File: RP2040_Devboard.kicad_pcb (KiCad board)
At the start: 2 copper layers, 42.2 x 59 mm, 47 parts, among them J1 USB_B_Mini, J2 Conn_01x03_Socket, J4 Conn_01x16, J6 Conn_01x16, SW1 SW_Push, SW2 SW_Push, U1 RP2040, U2 AP2112K-1.2, U3 USBLC6-2SC6, U4 W25Q128JVS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

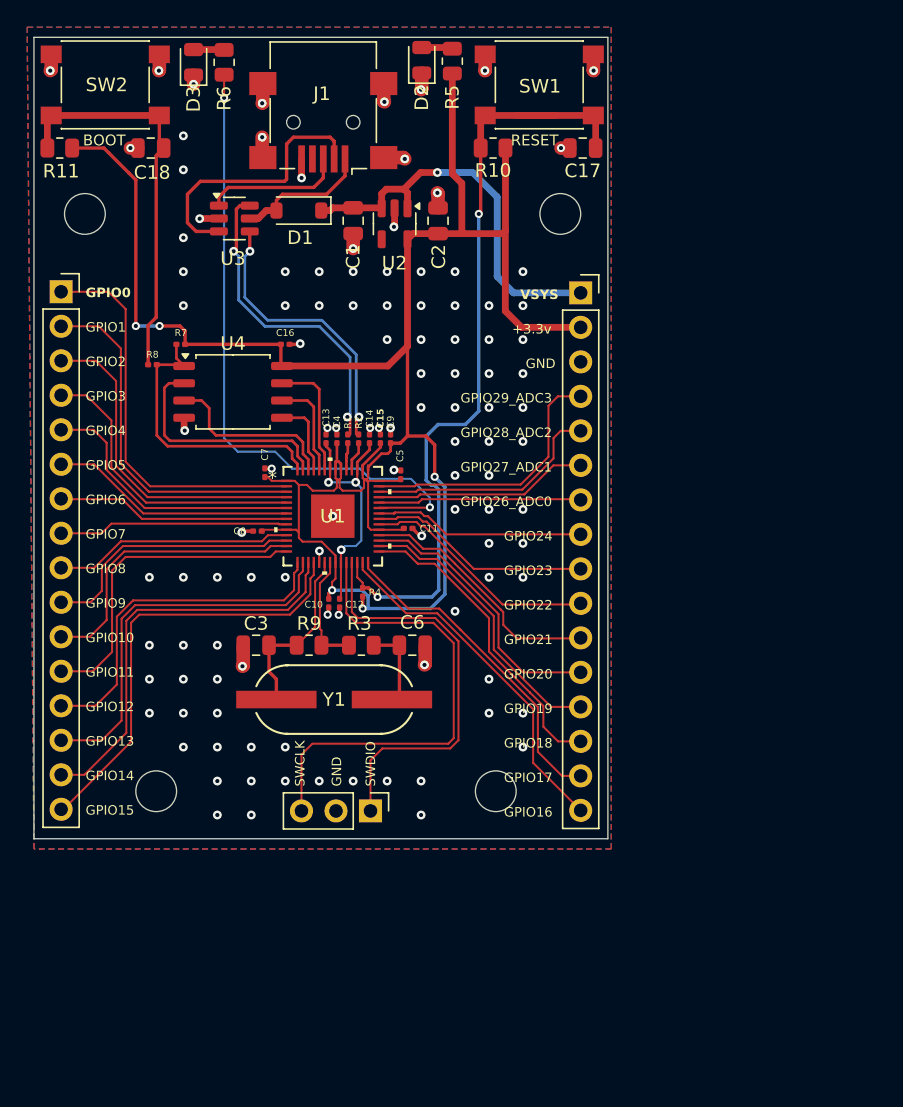
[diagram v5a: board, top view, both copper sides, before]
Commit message: Added board version
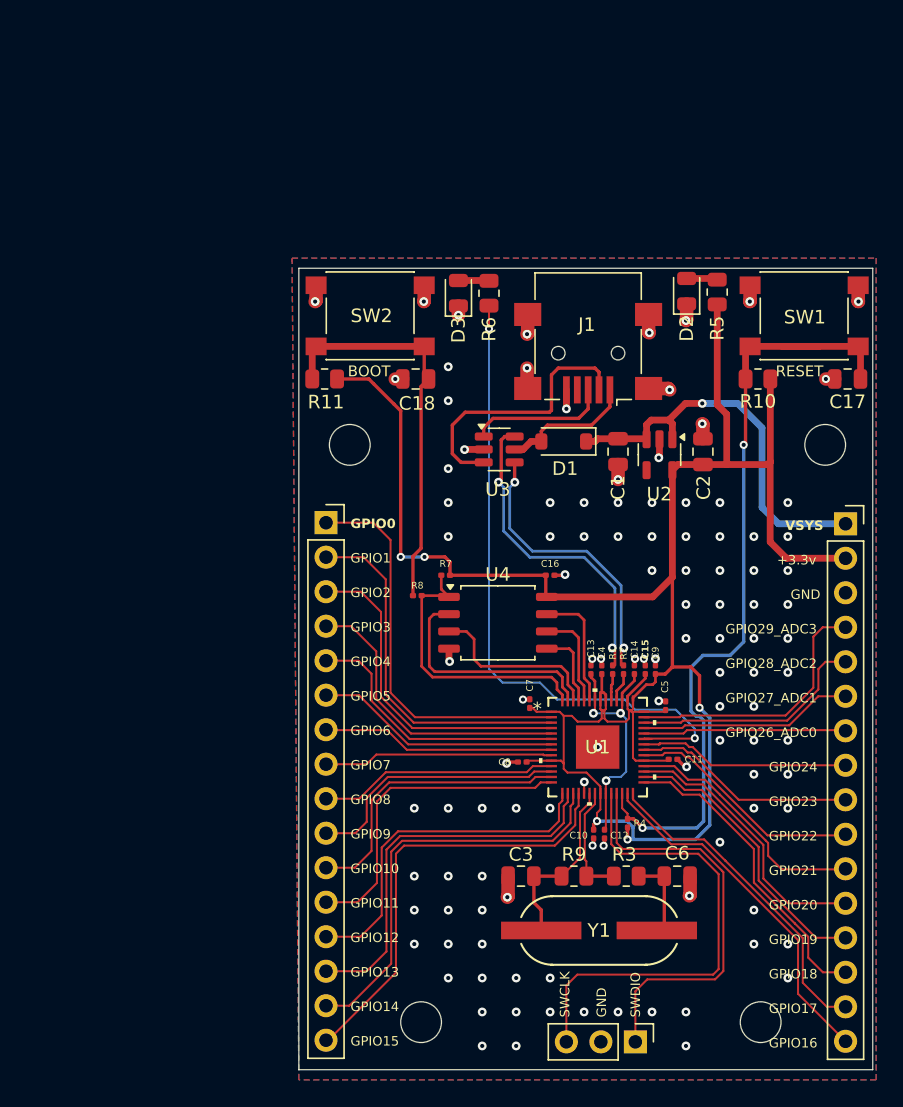
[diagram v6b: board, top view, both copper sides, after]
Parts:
- moved C16 25.9 mm to (142.0, 99.8)
- moved J1 25.9 mm to (144.8, 83.5)
- moved R2 25.9 mm to (147.4, 106.8)
- moved R7 25.9 mm to (134.3, 99.8)
- moved R9 25.9 mm to (143.8, 122.0)
- moved U4 25.9 mm to (138.2, 103.3)
- moved D3 25.9 mm to (135.2, 79.1)
- moved R6 25.9 mm to (137.5, 79.1)
- moved C1 25.9 mm to (147.0, 90.8)
- moved C10 25.9 mm to (145.2, 118.9)
- moved C11 25.9 mm to (151.0, 113.4)
- moved C12 25.9 mm to (146.0, 118.9)
- moved C13 25.9 mm to (145.0, 106.8)
- moved C14 25.9 mm to (148.2, 106.8)
- moved C15 25.9 mm to (149.0, 106.8)
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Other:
- board text added: "RP2040 Devboard v0.1"
